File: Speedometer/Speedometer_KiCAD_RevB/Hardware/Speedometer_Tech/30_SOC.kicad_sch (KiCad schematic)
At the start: 17 parts, among them U300 WS2812B-4020_2, U301 WS2812B-4020_2, U302 WS2812B-4020_2, U303 WS2812B-4020_2, U304 WS2812B-4020_2, U305 WS2812B-4020_2, U306 WS2812B-4020_2, U307 WS2812B-4020_2, U310 WS2812B-4020_2, U311 WS2812B-4020_2, U312 WS2812B-4020_2, U313 WS2812B-4020_2, U314 WS2812B-4020_2, U320 WS2812B-4020_2, U321 WS2812B-4020_2, U322 WS2812B-4020_2, U323 WS2812B-4020_2

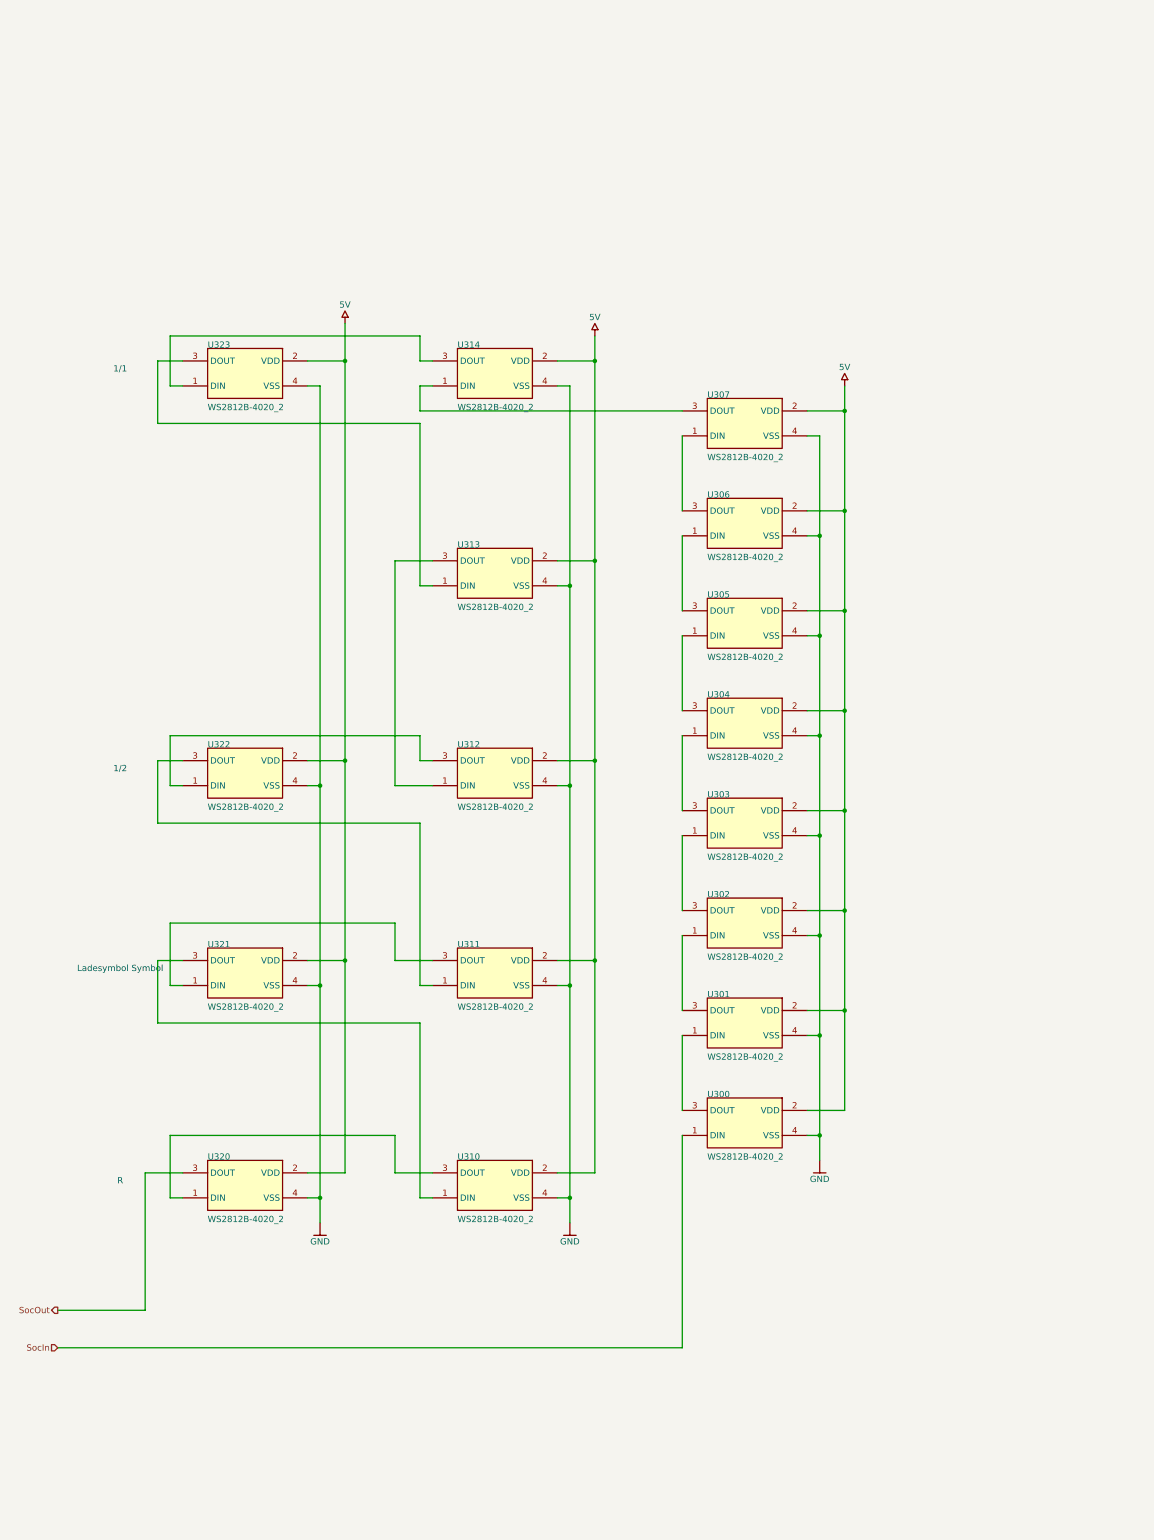
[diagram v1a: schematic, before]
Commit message: current version of lada speedometer in kicad
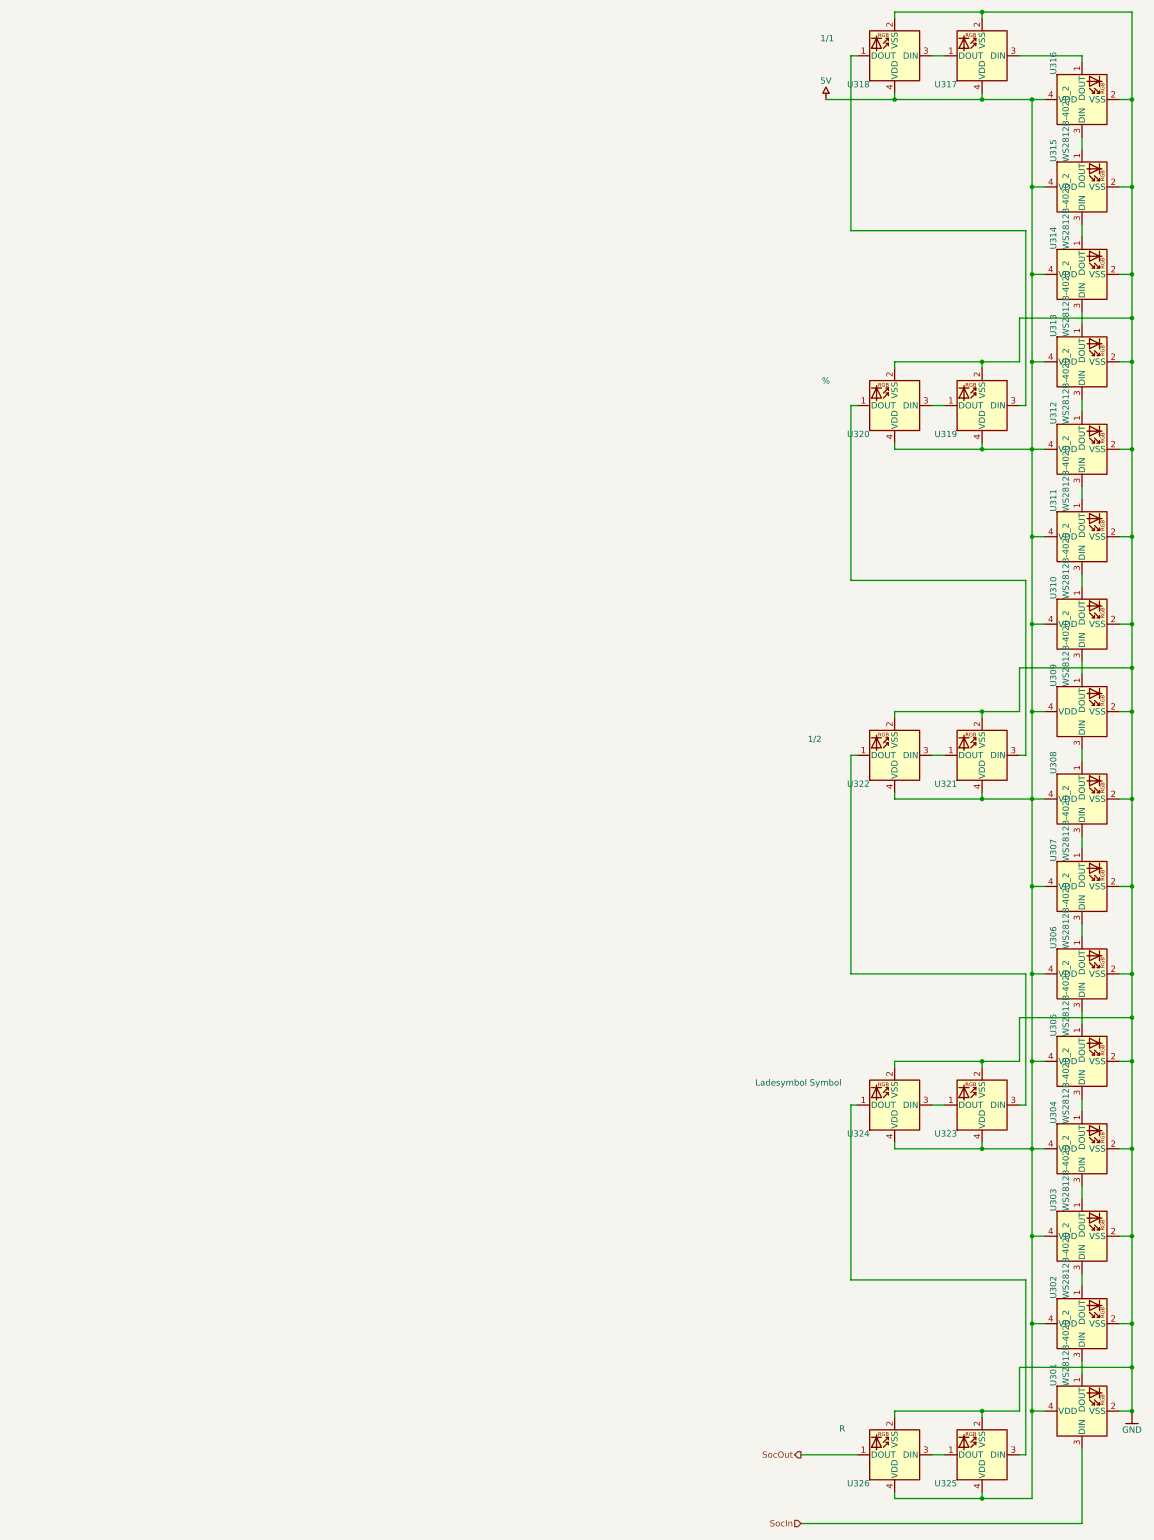
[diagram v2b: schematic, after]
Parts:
- removed U300, U301, U302, U303, U304, U305, U306, U307, U310, U311, U312, U313, U314, U320, U321, U322, U323: WS2812B-4020_2, LED_WS2812B-4020, symbol Speedometer_Tech-altium-import:Designator_0_WS2812B-4020_2
- added U301, U302, U303, U304, U305, U306, U307, U308, U309, U310, U311, U312, U313, U314, U315, U316, U317, U318, U319, U320, U321, U322, U323, U324, U325, U326: WS2812B-4020_2, LED_SMD:LED_WS2812B-2020_PLCC4_2.0x2.0mm, symbol LED:WS2812B-2020
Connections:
- net 5V: now also U301.4 (VDD), U302.4 (VDD), U303.4 (VDD), U304.4 (VDD), U305.4 (VDD), U306.4 (VDD), U307.4 (VDD), U308.4 (VDD), U309.4 (VDD), U310.4 (VDD), U311.4 (VDD), U312.4 (VDD), U313.4 (VDD), U314.4 (VDD), U315.4 (VDD), U316.4 (VDD), U317.4 (VDD), U318.4 (VDD), U319.4 (VDD), U320.4 (VDD), U321.4 (VDD), U322.4 (VDD), U323.4 (VDD), U324.4 (VDD), U325.4 (VDD), U326.4 (VDD)
- net GND: now also U301.2 (VSS), U302.2 (VSS), U303.2 (VSS), U304.2 (VSS), U305.2 (VSS), U306.2 (VSS), U307.2 (VSS), U308.2 (VSS), U309.2 (VSS), U310.2 (VSS), U311.2 (VSS), U312.2 (VSS), U313.2 (VSS), U314.2 (VSS), U315.2 (VSS), U316.2 (VSS), U317.2 (VSS), U318.2 (VSS), U319.2 (VSS), U320.2 (VSS), U321.2 (VSS), U322.2 (VSS), U323.2 (VSS), U324.2 (VSS), U325.2 (VSS), U326.2 (VSS)
- net SocIn: now also U301.3 (DIN)
- net SocOut: now also U326.1 (DOUT)
- new net: U312.1 (DOUT), U313.3 (DIN)
- new net: U311.1 (DOUT), U312.3 (DIN)
- new net: U301.1 (DOUT), U302.3 (DIN)
- new net: U325.1 (DOUT), U326.3 (DIN)
- new net: U322.1 (DOUT), U323.3 (DIN)
- new net: U321.1 (DOUT), U322.3 (DIN)
- new net: U324.1 (DOUT), U325.3 (DIN)
- new net: U323.1 (DOUT), U324.3 (DIN)
- new net: U320.1 (DOUT), U321.3 (DIN)
- new net: U319.1 (DOUT), U320.3 (DIN)
- new net: U318.1 (DOUT), U319.3 (DIN)
- new net: U309.1 (DOUT), U310.3 (DIN)
- new net: U308.1 (DOUT), U309.3 (DIN)
- new net: U315.1 (DOUT), U316.3 (DIN)
- new net: U314.1 (DOUT), U315.3 (DIN)
- new net: U310.1 (DOUT), U311.3 (DIN)
- new net: U313.1 (DOUT), U314.3 (DIN)
- new net: U302.1 (DOUT), U303.3 (DIN)
- new net: U306.1 (DOUT), U307.3 (DIN)
- new net: U305.1 (DOUT), U306.3 (DIN)
- new net: U307.1 (DOUT), U308.3 (DIN)
- new net: U303.1 (DOUT), U304.3 (DIN)
- new net: U304.1 (DOUT), U305.3 (DIN)
- new net: U317.1 (DOUT), U318.3 (DIN)
- new net: U316.1 (DOUT), U317.3 (DIN)
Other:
- note added: "%"
